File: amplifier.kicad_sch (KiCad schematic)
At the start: 0 parts

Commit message: draft amplifier circuit
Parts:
- added C10, C13: 100µ, symbol Device:C
- added C11, C14, C16, C17: 100n, symbol Device:C
- added C12, C15: 1n, symbol Device:C
- added C6, C7, C8, C9: 1µ, symbol Device:C
- added R13, R15: 100k, symbol Device:R
- added R14: 10, symbol Device:R
- added R16: 1k, symbol Device:R
- added U4: TPA3111D1QPWPRQ1, 0__:SOP65P640X120-29N, symbol 0 __:TPA3111D1QPWPRQ1
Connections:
- new net: R15.2, R16.1, U4.1 (SD), U4.2 (FAULT)
- new net: C17.1, U4.22 (BSN_1), U4.26 (BSN_2)
- new net: C17.2, U4.23 (OUTN_1), U4.25 (OUTN_2)
- new net: R13.1, U4.14 (AVCC_2)
- new net: C7.2, R13.2, R14.1, U4.7 (AVCC_1)
- new net: C6.2, U4.10 (PLIMIT), U4.9 (GVDD)
- new net: C16.1, U4.17 (BSP_1), U4.21 (BSP_2)
- new net: C16.2, U4.18 (OUTP_1), U4.20 (OUTP_2)
- new net: C8.2, U4.12 (INP)
- new net: C9.1, U4.11 (INN)
- new net GND: C10.1, C11.1, C12.1, C13.1, C14.1, C15.1, C6.1, C7.1, C9.2, U4.19 (PGND_1), U4.24 (PGND_2), U4.29 (EP), U4.3 (GND_1), U4.4 (GND_2), U4.6 (GAIN1), U4.8 (AGND)
- new net VCC: C10.2, C11.2, C12.2, C13.2, C14.2, C15.2, R14.2, R15.1, U4.15 (PVCC_1), U4.16 (PVCC_2), U4.27 (PVCC_3), U4.28 (PVCC_4), U4.5 (GAIN0)
- new net ~{AmpSD}: R16.2

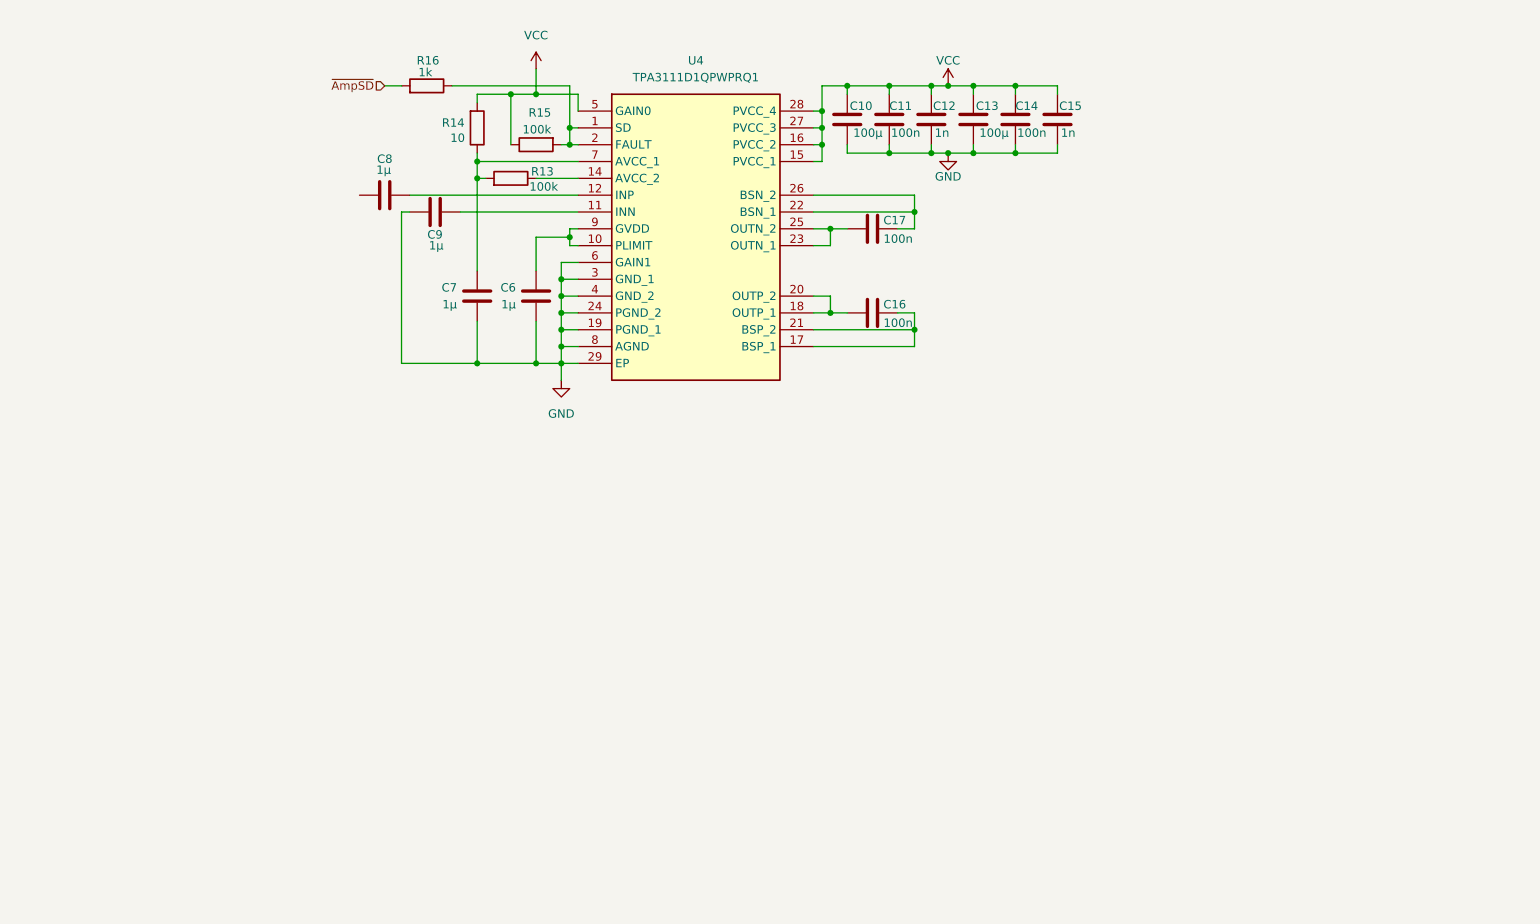
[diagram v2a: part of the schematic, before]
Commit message: Finish amplifier, add shutdown control
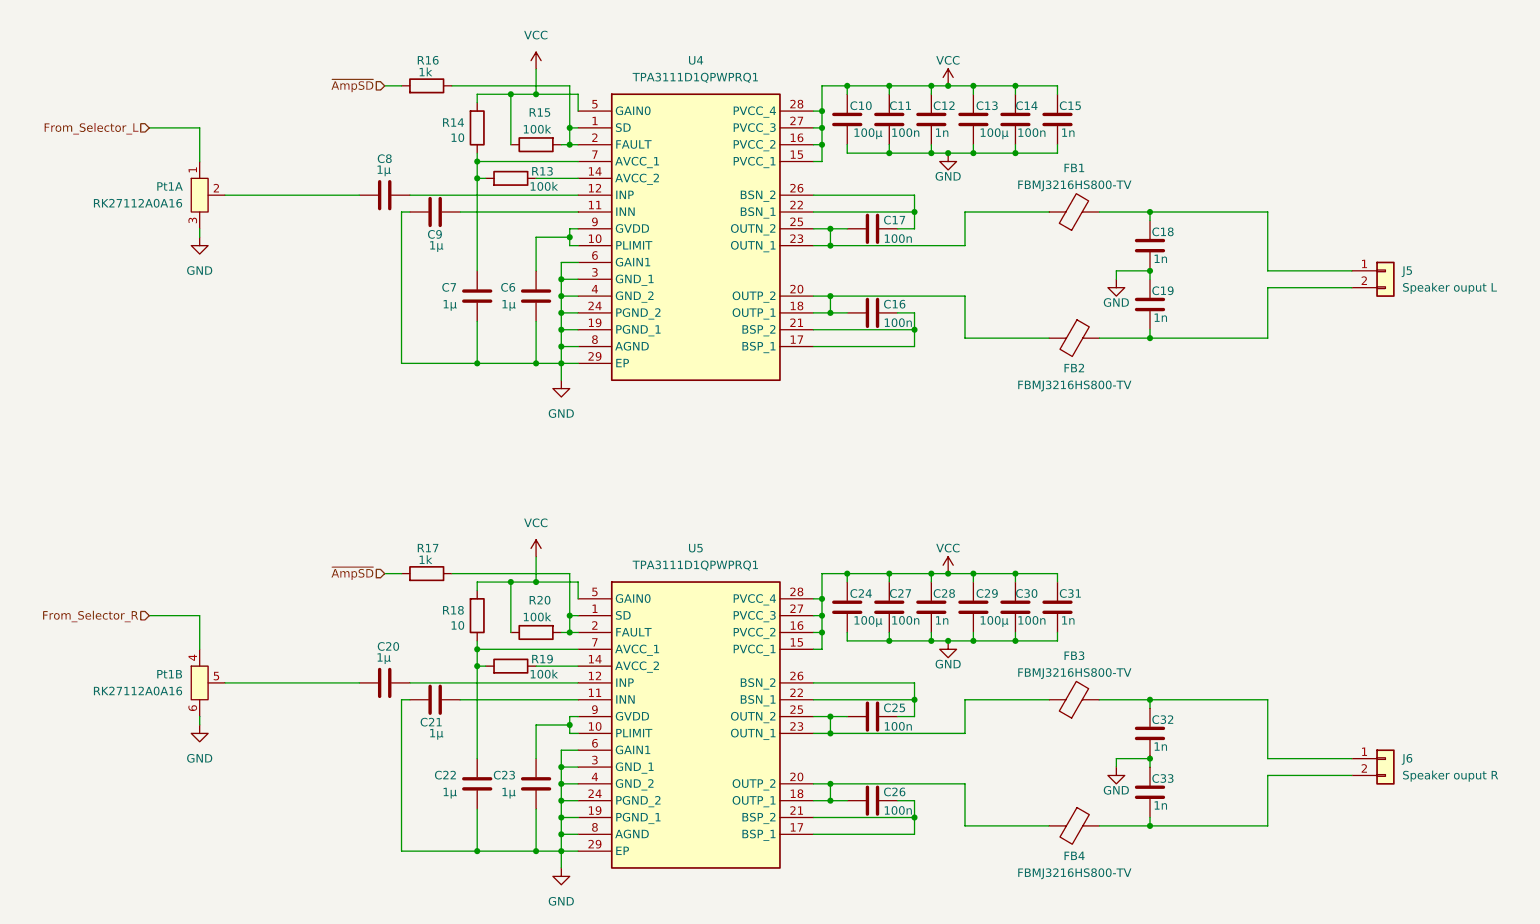
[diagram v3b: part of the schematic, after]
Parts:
- added C18, C19, C28, C31, C32, C33: 1n, symbol Device:C
- added C20, C21, C22, C23: 1µ, symbol Device:C
- added C24, C29: 100µ, symbol Device:C
- added C25, C26, C27, C30: 100n, symbol Device:C
- added FB1, FB2, FB3, FB4: FBMJ3216HS800-TV, symbol Device:FerriteBead
- added J5: Speaker ouput L, symbol Connector_Generic:Conn_01x02
- added J6: Speaker ouput R, symbol Connector_Generic:Conn_01x02
- added Pt1: RK27112A0A16, 0__:RES-ADJ-TH_RK27112A0A16, symbol 0 __:RK27112A0A16
- added R17: 1k, symbol Device:R
- added R18: 10, symbol Device:R
- added R19, R20: 100k, symbol Device:R
- added U5: TPA3111D1QPWPRQ1, 0__:SOP65P640X120-29N, symbol 0 __:TPA3111D1QPWPRQ1
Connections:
- net GND: now also C18.1, C19.2, C21.2, C22.1, C23.1, C24.1, C27.1, C28.1, C29.1, C30.1, C31.1, C32.1, C33.2, Pt1.3, Pt1.6, U5.19 (PGND_1), U5.24 (PGND_2), U5.29 (EP), U5.3 (GND_1), U5.4 (GND_2), U5.6 (GAIN1), U5.8 (AGND)
- net VCC: now also C24.2, C27.2, C28.2, C29.2, C30.2, C31.2, R18.2, R20.1, U5.15 (PVCC_1), U5.16 (PVCC_2), U5.27 (PVCC_3), U5.28 (PVCC_4), U5.5 (GAIN0)
- net ~{AmpSD}: now also R17.2
- net at C17.2, U4.23 (OUTN_1), U4.25 (OUTN_2): now also FB1.1
- net at C16.2, U4.18 (OUTP_1), U4.20 (OUTP_2): now also FB2.2
- net at C8.1: now also Pt1.2
- new net: C33.1, FB4.1, J6.2 (Pin_2)
- new net: C26.2, FB4.2, U5.18 (OUTP_1), U5.20 (OUTP_2)
- new net: C26.1, U5.17 (BSP_1), U5.21 (BSP_2)
- new net: R17.1, R20.2, U5.1 (SD), U5.2 (FAULT)
- new net: R19.1, U5.14 (AVCC_2)
- new net: C22.2, R18.1, R19.2, U5.7 (AVCC_1)
- new net: C18.2, FB1.2, J5.1 (Pin_1)
- new net: C25.2, FB3.1, U5.23 (OUTN_1), U5.25 (OUTN_2)
- new net: C32.2, FB3.2, J6.1 (Pin_1)
- new net: C19.1, FB2.1, J5.2 (Pin_2)
- new net: C25.1, U5.22 (BSN_1), U5.26 (BSN_2)
- new net: C23.2, U5.10 (PLIMIT), U5.9 (GVDD)
- new net: C21.1, U5.11 (INN)
- new net: C20.2, U5.12 (INP)
- new net: C20.1, Pt1.5
- new net From_Selector_L: Pt1.1
- new net From_Selector_R: Pt1.4

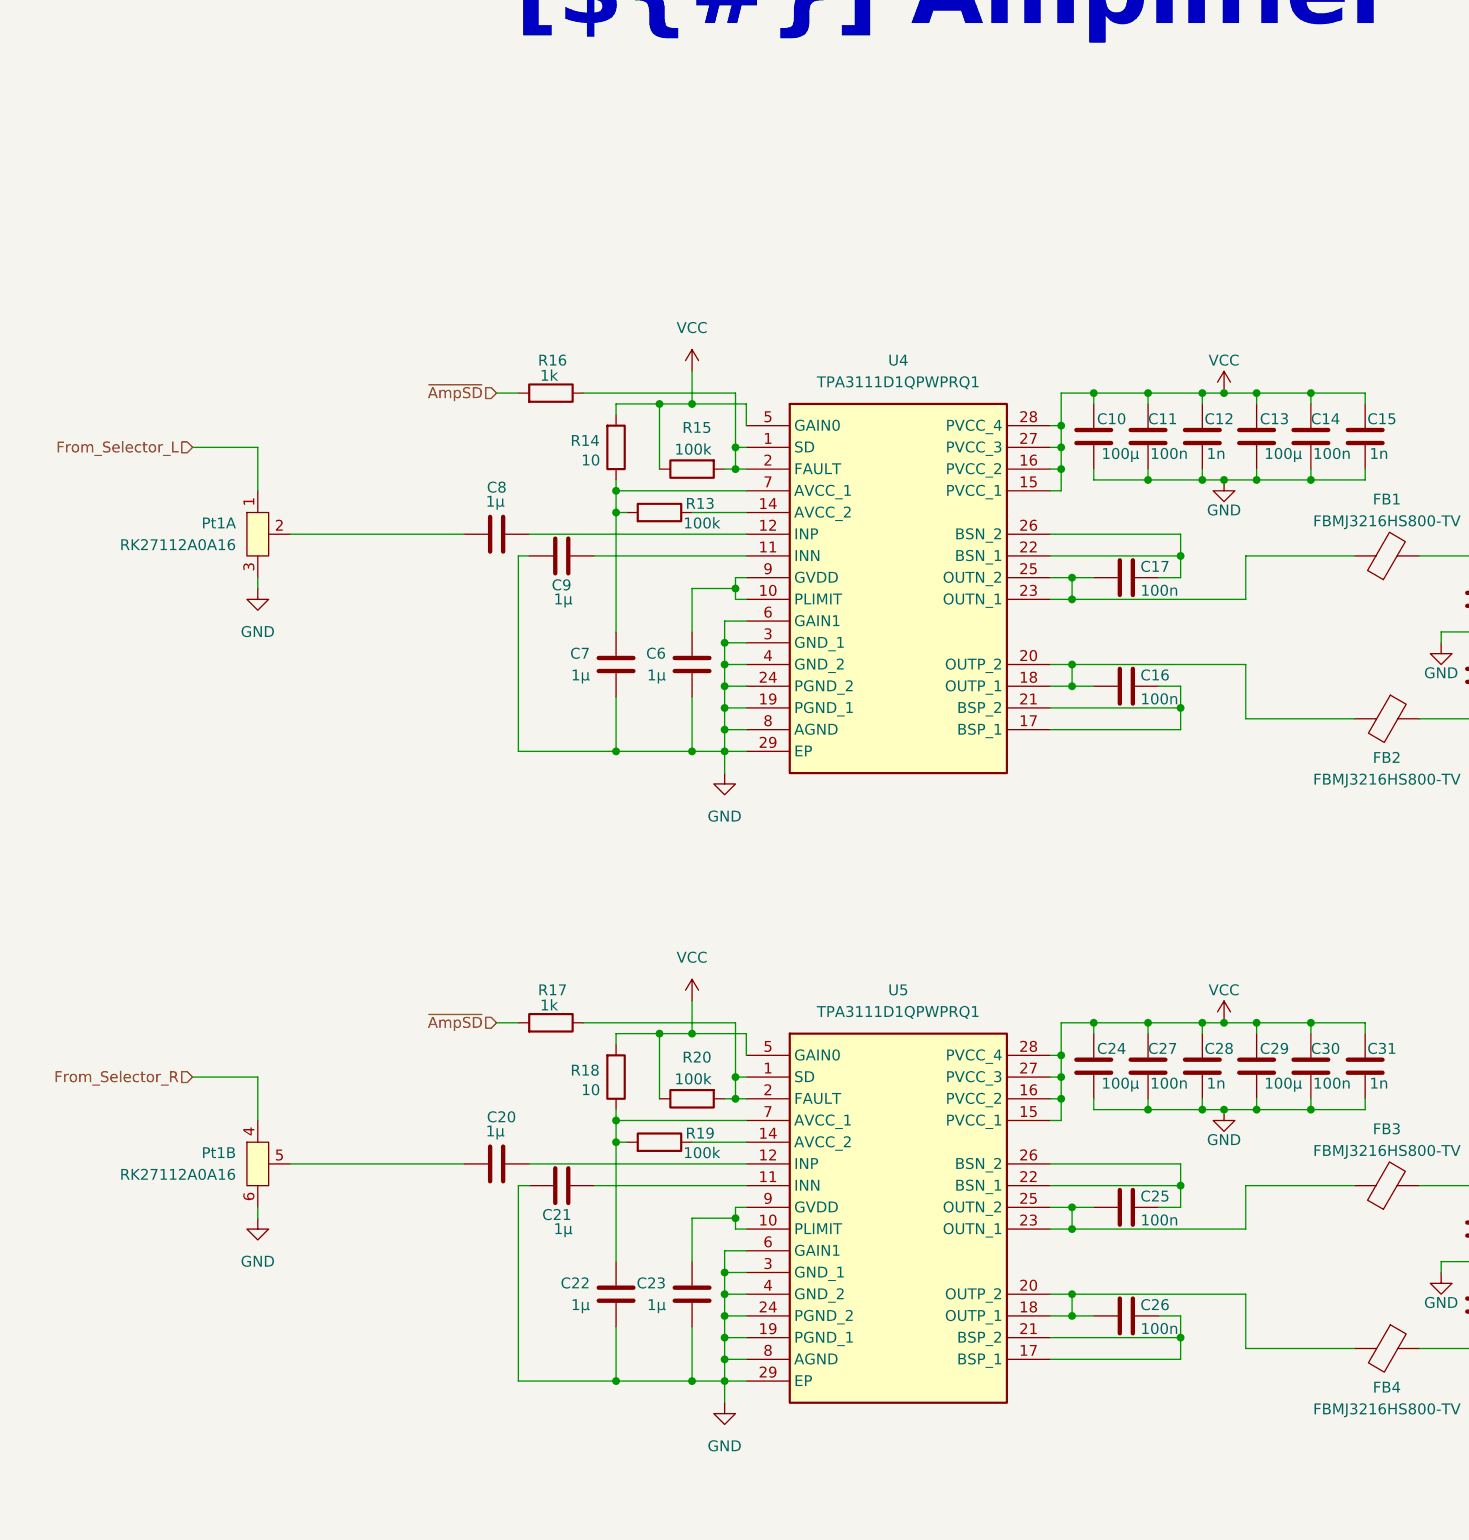
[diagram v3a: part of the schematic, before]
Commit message: change C10, C13, C24, C29 to polarized capacitor
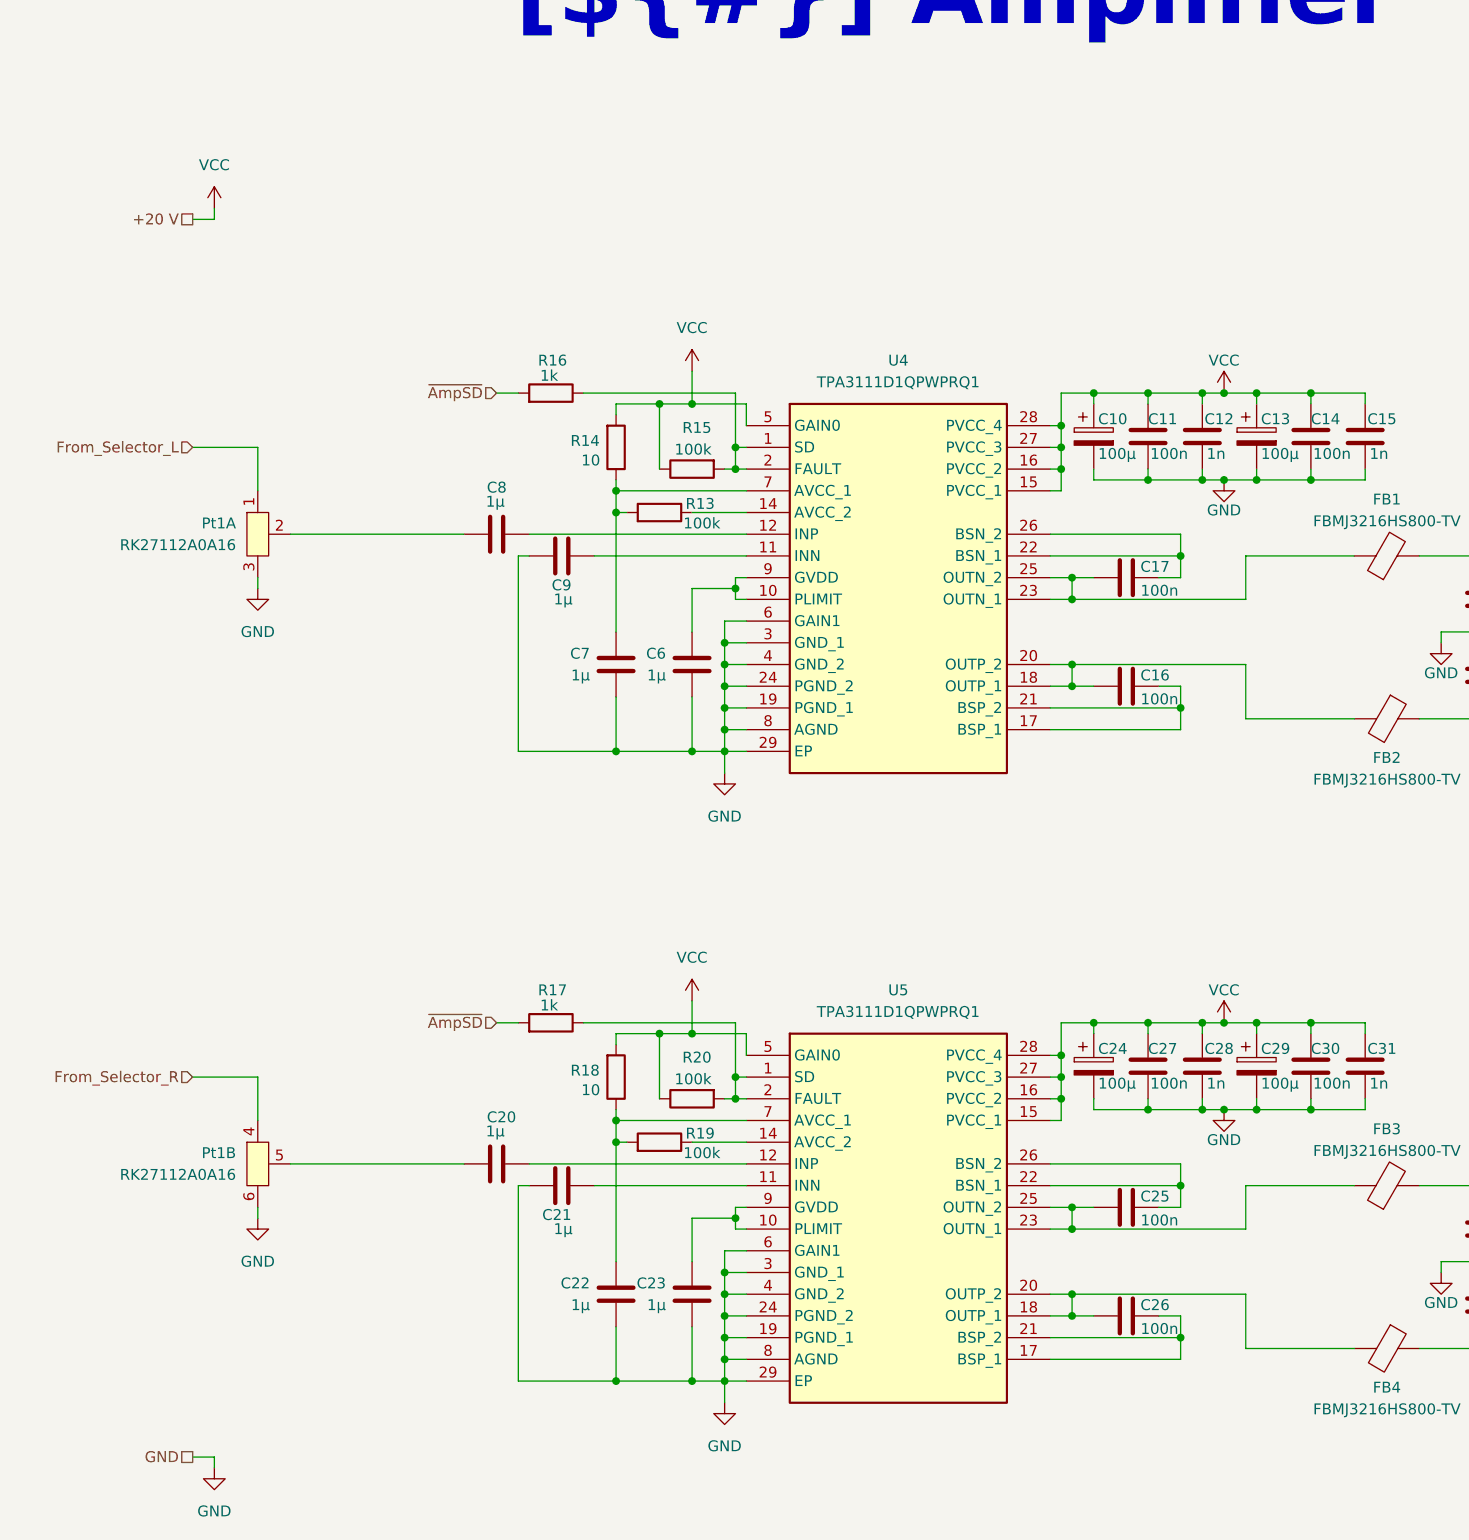
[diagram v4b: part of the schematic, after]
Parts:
- removed C10, C13, C24, C29: 100µ, symbol Device:C
- added C10, C13, C24, C29: 100µ, symbol Device:C_Polarized
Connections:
- net GND: now also C10.2, C13.2, C24.2, C29.2
- net VCC: now also C10.1, C13.1, C24.1, C29.1

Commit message: source component and fix some lib
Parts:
- C10, C13, C24, C29: footprint (none) -> Capacitor_SMD:CP_Elec_6.3x7.7; LCSC Part (none) -> C178585
- C11, C14, C16, C17, C25, C26, C27, C30: footprint (none) -> Capacitor_SMD:C_0402_1005Metric; LCSC Part (none) -> C77020
- C12, C15, C18, C19, C28, C31, C32, C33: footprint (none) -> Capacitor_SMD:C_0402_1005Metric; LCSC Part (none) -> C77018
- C20, C21, C22, C23, C6, C7, C8, C9: footprint (none) -> Capacitor_SMD:C_0402_1005Metric; LCSC Part (none) -> C1518208
- FB1, FB2, FB3, FB4: footprint (none) -> Inductor_SMD:L_1206_3216Metric; LCSC Part (none) -> C2661525
- J5, J6: footprint (none) -> Connector_PinHeader_2.54mm:PinHeader_1x02_P2.54mm_Vertical
- R13, R15, R19, R20: footprint (none) -> Resistor_SMD:R_0402_1005Metric; LCSC Part (none) -> C427253
- R14, R18: footprint (none) -> Resistor_SMD:R_0402_1005Metric; LCSC Part (none) -> C854481
- R16, R17: footprint (none) -> Resistor_SMD:R_0402_1005Metric; LCSC Part (none) -> C427241
- U4, U5: LCSC Part (none) -> C114457

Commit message: finish pcb and generate production file
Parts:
- renumbered C25 to C24, C26 to C25, C24 to C26
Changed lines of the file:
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@@
 		(on_board yes)
 		(dnp no)
-		(property "Reference" "C26"
+		(property "Reference" "C25"
 			(at 234.95 177.8 90)
 			(effects
@@
 			(project "AudioInterface"
 				(path "/0650c7a8-acba-429c-9f8e-eec0baf0bc1c/fede4c36-00cc-4d3d-b71c-5243ba232202/4ebd39c7-90aa-4c04-a136-f35dff148277"
-					(reference "C26")
+					(reference "C25")
 					(unit 1)
 				)
@@
 		(on_board yes)
 		(dnp no)
-		(property "Reference" "C24"
+		(property "Reference" "C26"
 			(at 226.568 147.828 0)
 			(effects
@@
 			(project "AudioInterface"
 				(path "/0650c7a8-acba-429c-9f8e-eec0baf0bc1c/fede4c36-00cc-4d3d-b71c-5243ba232202/4ebd39c7-90aa-4c04-a136-f35dff148277"
-					(reference "C24")
+					(reference "C26")
 					(unit 1)
 				)
@@
 		(on_board yes)
 		(dnp no)
-		(property "Reference" "C25"
+		(property "Reference" "C24"
 			(at 234.95 165.1 90)
 			(effects
@@
 			(project "AudioInterface"
 				(path "/0650c7a8-acba-429c-9f8e-eec0baf0bc1c/fede4c36-00cc-4d3d-b71c-5243ba232202/4ebd39c7-90aa-4c04-a136-f35dff148277"
-					(reference "C25")
-					(unit 1)
-				)
+					(reference "C24")
+					(unit 1)
+				)
